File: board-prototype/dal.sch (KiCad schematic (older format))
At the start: 9 parts, among them U101 Am2908, U102 Am2908, U103 Am2908, U104 Am2908, U105 Am2908, U106 Am2908, U107 74LVC7T245, U108 74LVC7T245, U109 74LVC7T245

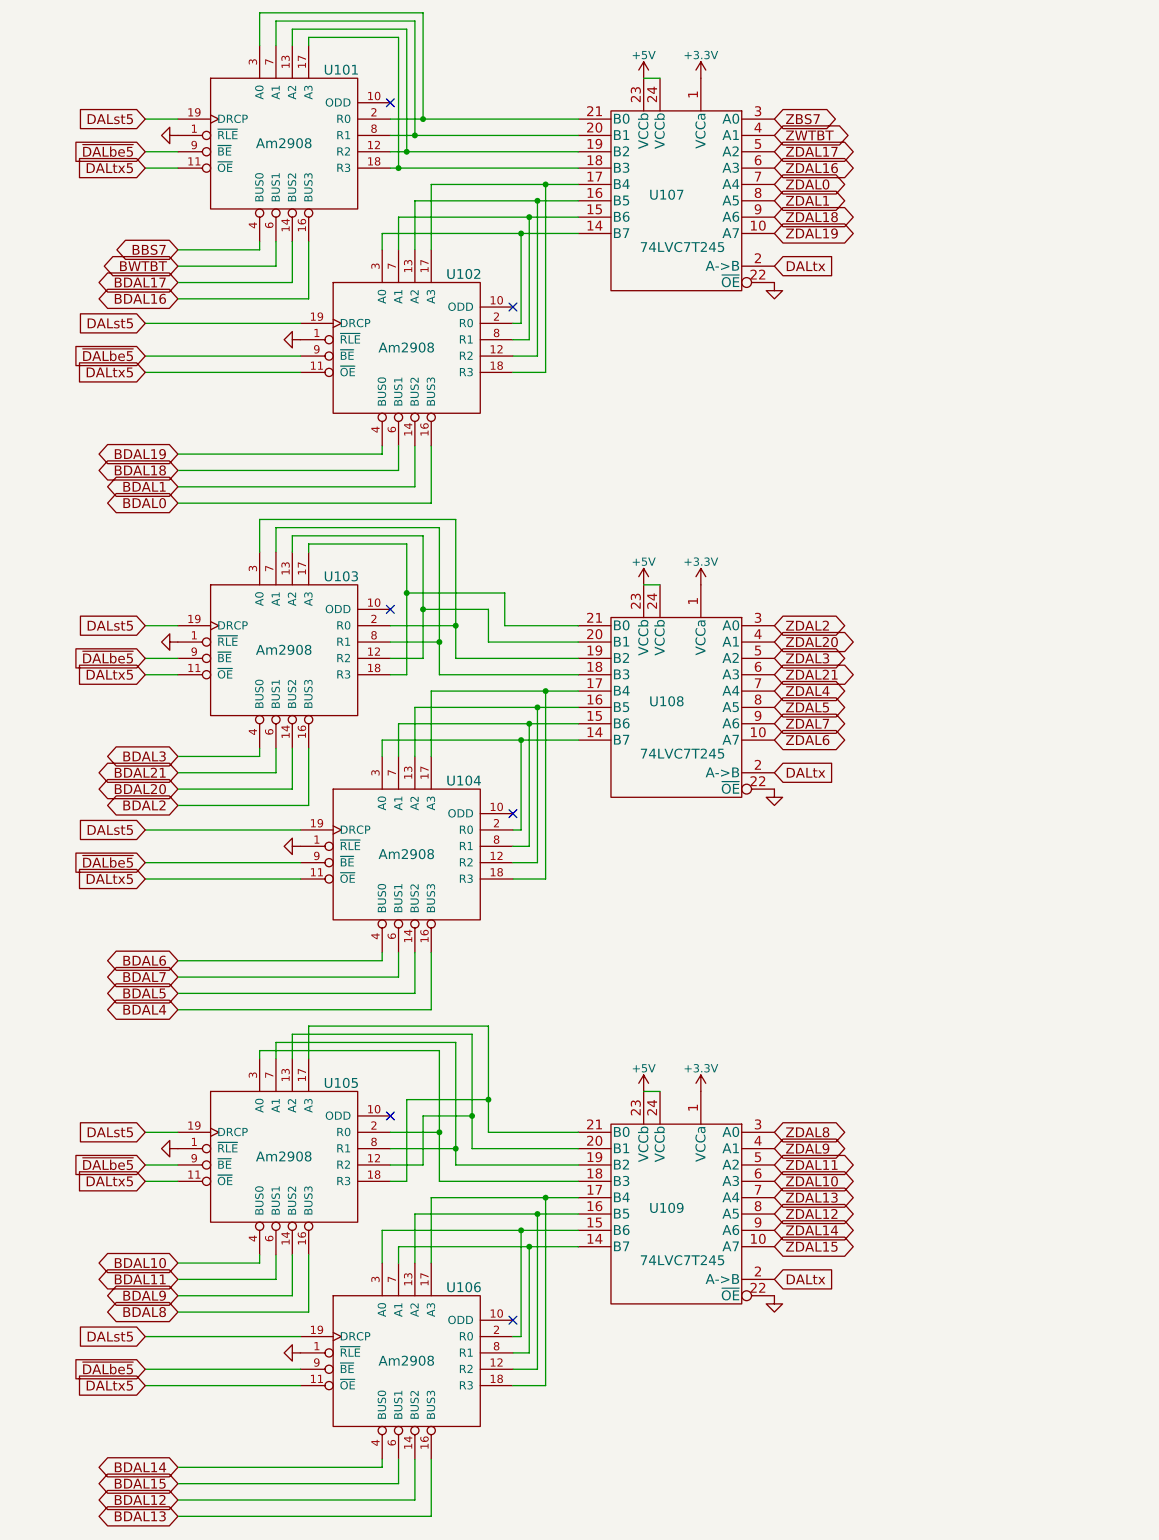
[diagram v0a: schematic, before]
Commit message: Changed over to only DS8641 bus transceivers and the smaller package level-converters.
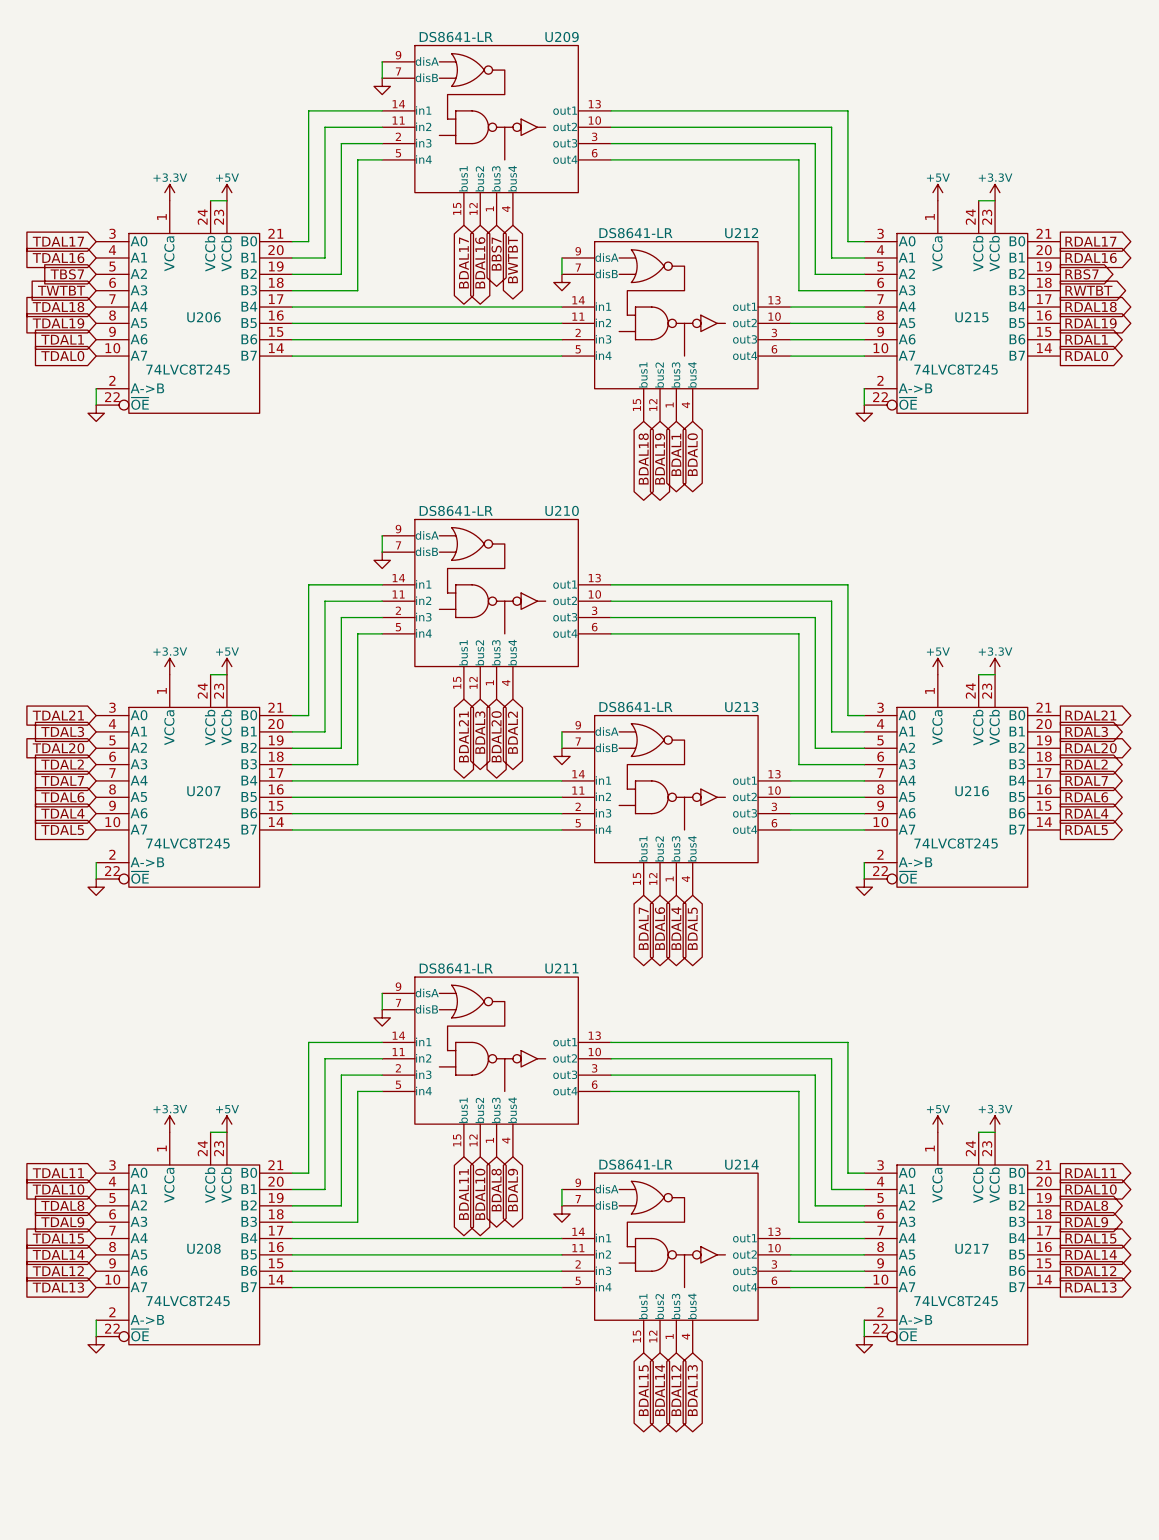
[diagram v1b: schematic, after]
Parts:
- removed U101, U102, U103, U104, U105, U106: Am2908, Sockets_DIP:DIP-20__300, symbol Am2908
- removed U107, U108, U109: 74LVC7T245, SMD_Packages:SOIC-24, symbol 74LVC7T245
- added U206, U207, U208, U215, U216, U217: 74LVC8T245, Housings_SSOP:TSSOP-24_4.4x7.8mm_Pitch0.65mm, symbol 74LVC8T245
- added U209, U210, U211, U212, U213, U214: DS8641-LR, Sockets_DIP:DIP-16__300, symbol DS8641-LR
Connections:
- net +3V3: now also U206.1 (VCCa), U207.1 (VCCa), U208.1 (VCCa), U215.23 (VCCb), U215.24 (VCCb), U216.23 (VCCb), U216.24 (VCCb), U217.23 (VCCb), U217.24 (VCCb)
- net +5V: now also U206.23 (VCCb), U206.24 (VCCb), U207.23 (VCCb), U207.24 (VCCb), U208.23 (VCCb), U208.24 (VCCb), U215.1 (VCCa), U216.1 (VCCa), U217.1 (VCCa)
- net BBS7: now also U209.1 (bus3)
- net BDAL0: now also U212.4 (bus4)
- net BDAL1: now also U212.1 (bus3)
- net BDAL10: now also U211.12 (bus2)
- net BDAL11: now also U211.15 (bus1)
- net BDAL12: now also U214.1 (bus3)
- net BDAL13: now also U214.4 (bus4)
- net BDAL14: now also U214.12 (bus2)
- net BDAL15: now also U214.15 (bus1)
- net BDAL16: now also U209.12 (bus2)
- net BDAL17: now also U209.15 (bus1)
- net BDAL18: now also U212.15 (bus1)
- net BDAL19: now also U212.12 (bus2)
- net BDAL2: now also U210.4 (bus4)
- net BDAL20: now also U210.1 (bus3)
- net BDAL21: now also U210.15 (bus1)
- net BDAL3: now also U210.12 (bus2)
- net BDAL4: now also U213.1 (bus3)
- net BDAL5: now also U213.4 (bus4)
- net BDAL6: now also U213.12 (bus2)
- net BDAL7: now also U213.15 (bus1)
- net BDAL8: now also U211.1 (bus3)
- net BDAL9: now also U211.4 (bus4)
- net BWTBT: now also U209.4 (bus4)
- net GND: now also U206.11 (GND), U206.12 (GND), U206.13 (GND), U206.2 (A->B), U206.22 (~OE), U207.11 (GND), U207.12 (GND), U207.13 (GND), U207.2 (A->B), U207.22 (~OE), U208.11 (GND), U208.12 (GND), U208.13 (GND), U208.2 (A->B), U208.22 (~OE), U209.7 (disB), U209.8 (GND), U209.9 (disA), U210.7 (disB), U210.8 (GND), U210.9 (disA), U211.7 (disB), U211.8 (GND), U211.9 (disA), U212.7 (disB), U212.8 (GND), U212.9 (disA), U213.7 (disB), U213.8 (GND), U213.9 (disA), U214.7 (disB), U214.8 (GND), U214.9 (disA), U215.11 (GND), U215.12 (GND), U215.13 (GND), U215.2 (A->B), U215.22 (~OE), U216.11 (GND), U216.12 (GND), U216.13 (GND), U216.2 (A->B), U216.22 (~OE), U217.11 (GND), U217.12 (GND), U217.13 (GND), U217.2 (A->B), U217.22 (~OE)
- net VCC: now also U209.16 (VCC), U210.16 (VCC), U211.16 (VCC), U212.16 (VCC), U213.16 (VCC), U214.16 (VCC)
- new net: U209.10 (out2), U215.4 (A1)
- new net: U206.20 (B1), U209.11 (in2)
- new net: U209.13 (out1), U215.3 (A0)
- new net: U206.21 (B0), U209.14 (in1)
- new net: U206.19 (B2), U209.2 (in3)
- new net: U209.3 (out3), U215.5 (A2)
- new net: U206.18 (B3), U209.5 (in4)
- new net: U209.6 (out4), U215.6 (A3)
- new net: U212.10 (out2), U215.8 (A5)
- new net: U206.16 (B5), U212.11 (in2)
- new net: U212.13 (out1), U215.7 (A4)
- new net: U206.17 (B4), U212.14 (in1)
- new net: U206.15 (B6), U212.2 (in3)
- new net: U212.3 (out3), U215.9 (A6)
- new net: U206.14 (B7), U212.5 (in4)
- new net: U212.6 (out4), U215.10 (A7)
- new net: U210.10 (out2), U216.4 (A1)
- new net: U207.20 (B1), U210.11 (in2)
- new net: U210.13 (out1), U216.3 (A0)
- new net: U207.21 (B0), U210.14 (in1)
- new net: U207.19 (B2), U210.2 (in3)
- new net: U210.3 (out3), U216.5 (A2)
- new net: U207.18 (B3), U210.5 (in4)
- new net: U210.6 (out4), U216.6 (A3)
- new net: U213.10 (out2), U216.8 (A5)
- new net: U207.16 (B5), U213.11 (in2)
- new net: U213.13 (out1), U216.7 (A4)
- new net: U207.17 (B4), U213.14 (in1)
- new net: U207.15 (B6), U213.2 (in3)
- new net: U213.3 (out3), U216.9 (A6)
- new net: U207.14 (B7), U213.5 (in4)
- new net: U213.6 (out4), U216.10 (A7)
- new net: U211.10 (out2), U217.4 (A1)
- new net: U208.20 (B1), U211.11 (in2)
- new net: U211.13 (out1), U217.3 (A0)
- new net: U208.21 (B0), U211.14 (in1)
- new net: U208.19 (B2), U211.2 (in3)
- new net: U211.3 (out3), U217.5 (A2)
- new net: U208.18 (B3), U211.5 (in4)
- new net: U211.6 (out4), U217.6 (A3)
- new net: U214.10 (out2), U217.8 (A5)
- new net: U208.16 (B5), U214.11 (in2)
- new net: U214.13 (out1), U217.7 (A4)
- new net: U208.17 (B4), U214.14 (in1)
- new net: U208.15 (B6), U214.2 (in3)
- new net: U214.3 (out3), U217.9 (A6)
- new net: U208.14 (B7), U214.5 (in4)
- new net: U214.6 (out4), U217.10 (A7)
- new net RBS7: U215.19 (B2)
- new net RDAL0: U215.14 (B7)
- new net RDAL1: U215.15 (B6)
- new net RDAL10: U217.20 (B1)
- new net RDAL11: U217.21 (B0)
- new net RDAL12: U217.15 (B6)
- new net RDAL13: U217.14 (B7)
- new net RDAL14: U217.16 (B5)
- new net RDAL15: U217.17 (B4)
- new net RDAL16: U215.20 (B1)
- new net RDAL17: U215.21 (B0)
- new net RDAL18: U215.17 (B4)
- new net RDAL19: U215.16 (B5)
- new net RDAL2: U216.18 (B3)
- new net RDAL20: U216.19 (B2)
- new net RDAL21: U216.21 (B0)
- new net RDAL3: U216.20 (B1)
- new net RDAL4: U216.15 (B6)
- new net RDAL5: U216.14 (B7)
- new net RDAL6: U216.16 (B5)
- new net RDAL7: U216.17 (B4)
- new net RDAL8: U217.19 (B2)
- new net RDAL9: U217.18 (B3)
- new net RWTBT: U215.18 (B3)
- new net TBS7: U206.5 (A2)
- new net TDAL0: U206.10 (A7)
- new net TDAL1: U206.9 (A6)
- new net TDAL10: U208.4 (A1)
- new net TDAL11: U208.3 (A0)
- new net TDAL12: U208.9 (A6)
- new net TDAL13: U208.10 (A7)
- new net TDAL14: U208.8 (A5)
- new net TDAL15: U208.7 (A4)
- new net TDAL16: U206.4 (A1)
- new net TDAL17: U206.3 (A0)
- new net TDAL18: U206.7 (A4)
- new net TDAL19: U206.8 (A5)
- new net TDAL2: U207.6 (A3)
- new net TDAL20: U207.5 (A2)
- new net TDAL21: U207.3 (A0)
- new net TDAL3: U207.4 (A1)
- new net TDAL4: U207.9 (A6)
- new net TDAL5: U207.10 (A7)
- new net TDAL6: U207.8 (A5)
- new net TDAL7: U207.7 (A4)
- new net TDAL8: U208.5 (A2)
- new net TDAL9: U208.6 (A3)
- new net TWTBT: U206.6 (A3)
- no-connect marks 6 -> 0

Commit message: Updated to KiCad 5
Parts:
- U206, U207, U208, U215, U216, U217: symbol 74LVC8T245 -> myLib:74LVC8T245
- U209, U210, U211, U212, U213, U214: symbol DS8641-LR -> myLib:DS8641-LR
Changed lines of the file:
@@
-EESchema Schematic File Version 2
-LIBS:power
-LIBS:device
-LIBS:transistors
-LIBS:conn
-LIBS:linear
-LIBS:regul
-LIBS:74xx
-LIBS:cmos4000
-LIBS:adc-dac
-LIBS:memory
-LIBS:xilinx
-LIBS:microcontrollers
-LIBS:dsp
-LIBS:microchip
-LIBS:analog_switches
-LIBS:motorola
-LIBS:texas
-LIBS:intel
-LIBS:audio
-LIBS:interface
-LIBS:digital-audio
-LIBS:philips
-LIBS:display
-LIBS:cypress
-LIBS:siliconi
-LIBS:opto
-LIBS:atmel
-LIBS:contrib
-LIBS:valves
-LIBS:myLib
+EESchema Schematic File Version 4
 LIBS:proto-cache
-EELAYER 25 0
+EELAYER 26 0
 EELAYER END
 $Descr USLetter 8500 11000 portrait
@@
 $EndDescr
 $Comp
-L GND #PWR071
+L power:GND #PWR071
 U 1 1 56BE727C
 P 1300 2950
@@
 $EndComp
 $Comp
-L +5V #PWR072
+L power:+5V #PWR072
 U 1 1 56BE7282
 P 2100 1700
@@
 $EndComp
 $Comp
-L +3.3V #PWR073
+L power:+3.3V #PWR073
 U 1 1 56BE7288
 P 1750 1700
@@
 $EndComp
 $Comp
-L +5V #PWR074
+L power:+5V #PWR074
 U 1 1 56BE729B
 P 6450 4600
@@
 $EndComp
 $Comp
-L +3.3V #PWR075
+L power:+3.3V #PWR075
 U 1 1 56BE72A1
 P 6800 4600
@@
 $EndComp
 $Comp
-L +5V #PWR076
+L power:+5V #PWR076
 U 1 1 56BE72B4
 P 6450 7400
@@
 $EndComp
 $Comp
-L +3.3V #PWR077
+L power:+3.3V #PWR077
 U 1 1 56BE72BA
 P 6800 7400
@@
 BWTBT
 $Comp
-L GND #PWR078
+L power:GND #PWR078
 U 1 1 56BEDAD0
 P 6000 5850
@@
 $EndComp
 $Comp
-L GND #PWR079
+L power:GND #PWR079
 U 1 1 56BEDB08
 P 6000 8650
@@
 $EndComp
 $Comp
-L DS8641-LR U209
+L myLib:DS8641-LR U209
 U 1 1 56CE4104
 P 3750 1450
@@
 $EndComp
 $Comp
-L DS8641-LR U212
+L myLib:DS8641-LR U212
 U 1 1 56CE4226
 P 4850 2650
@@
 	1300 2850 1300 2950
 $Comp
-L GND #PWR080
+L power:GND #PWR080
 U 1 1 56CE453B
 P 6000 2950
@@
 $EndComp
 $Comp
-L +5V #PWR081
+L power:+5V #PWR081
 U 1 1 56CE4541
 P 6450 1700
@@
 $EndComp
 $Comp
-L +3.3V #PWR082
+L power:+3.3V #PWR082
 U 1 1 56CE4547
 P 6800 1700
@@
 	6000 8550 6000 8650
 $Comp
-L +5V #PWR083
+L power:+5V #PWR083
 U 1 1 56CE46AF
 P 2100 7400
@@
 $EndComp
 $Comp
-L +3.3V #PWR084
+L power:+3.3V #PWR084
 U 1 1 56CE46B5
 P 1750 7400
@@
 	2000 7400 2100 7400
 $Comp
-L GND #PWR085
+L power:GND #PWR085
 U 1 1 56CE46C4
 P 1300 8650
@@
 	6000 5750 6000 5850
 $Comp
-L +5V #PWR086
+L power:+5V #PWR086
 U 1 1 56CE484A
 P 2100 4600
@@
 $EndComp
 $Comp
-L +3.3V #PWR087
+L power:+3.3V #PWR087
 U 1 1 56CE4850
 P 1750 4600
@@
 	2000 4600 2100 4600
 $Comp
-L GND #PWR088
+L power:GND #PWR088
 U 1 1 56CE485F
 P 1300 5850
@@
 	1300 5750 1300 5850
 $Comp
-L GND #PWR089
+L power:GND #PWR089
 U 1 1 56CE4E7B
 P 3050 950
@@
 	4150 2050 4150 2150
 $Comp
-L GND #PWR090
+L power:GND #PWR090
 U 1 1 56CE4F4D
 P 4150 2150
@@
 $EndComp
 $Comp
-L DS8641-LR U210
+L myLib:DS8641-LR U210
 U 1 1 56CE4FC4
 P 3750 4350
@@
 $EndComp
 $Comp
-L DS8641-LR U213
+L myLib:DS8641-LR U213
 U 1 1 56CE4FCA
 P 4850 5550
@@
 $EndComp
 $Comp
-L GND #PWR091
+L power:GND #PWR091
 U 1 1 56CE4FD0
 P 3050 3850
@@
 	4150 4950 4150 5050
 $Comp
-L GND #PWR092
+L power:GND #PWR092
 U 1 1 56CE4FD8
 P 4150 5050
@@
 $EndComp
 $Comp
-L DS8641-LR U211
+L myLib:DS8641-LR U211
 U 1 1 56CE50C0
 P 3750 7150
@@
 $EndComp
 $Comp
-L DS8641-LR U214
+L myLib:DS8641-LR U214
 U 1 1 56CE50C6
 P 4850 8350
@@
 $EndComp
 $Comp
-L GND #PWR093
+L power:GND #PWR093
 U 1 1 56CE50CC
 P 3050 6650
@@
 	4150 7750 4150 7850
 $Comp
-L GND #PWR094
+L power:GND #PWR094
 U 1 1 56CE50D4
 P 4150 7850
@@
 	4150 2650 2500 2650
 $Comp
-L 74LVC8T245 U215
+L myLib:74LVC8T245 U215
 U 1 1 580E28F1
 P 6600 2450
@@
 $EndComp
 $Comp
-L 74LVC8T245 U216
+L myLib:74LVC8T245 U216
 U 1 1 580E29B6
 P 6600 5350
@@
 $EndComp
 $Comp
-L 74LVC8T245 U217
+L myLib:74LVC8T245 U217
 U 1 1 580E2A12
 P 6600 8150
@@
 $EndComp
 $Comp
-L 74LVC8T245 U206
+L myLib:74LVC8T245 U206
 U 1 1 580E2D1F
 P 1900 2450
@@
 $EndComp
 $Comp
-L 74LVC8T245 U208
+L myLib:74LVC8T245 U208
 U 1 1 580E2D91
 P 1900 8150
@@
 $EndComp
 $Comp
-L 74LVC8T245 U207
+L myLib:74LVC8T245 U207
 U 1 1 580E2E00
 P 1900 5350
